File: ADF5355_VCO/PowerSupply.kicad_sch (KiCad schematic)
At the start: 15 parts, among them IC1 ADM7150ACPZ-3.3-R7, IC2 ADM7150ARDZ-5.0, U3 TPS7A0533PDBZ

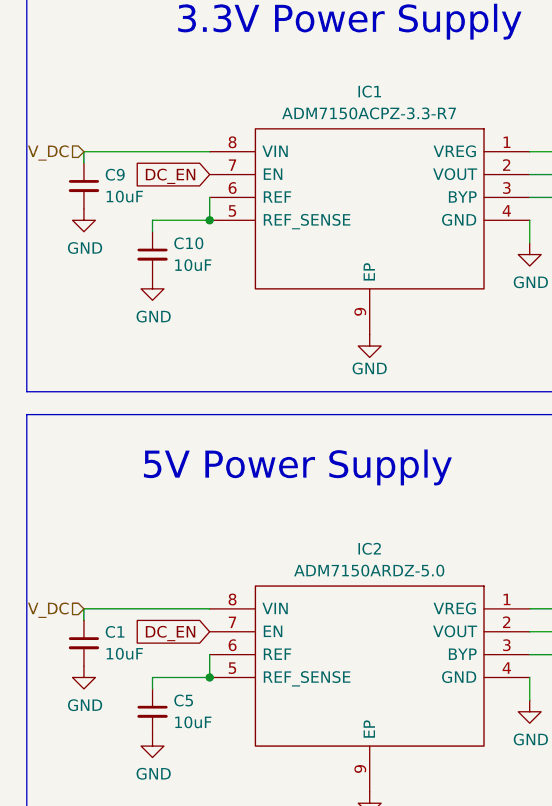
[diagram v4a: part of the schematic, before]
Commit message: Added additional footprints and BOM
Added a bill of materials with most of the components.
Added footprints for more components
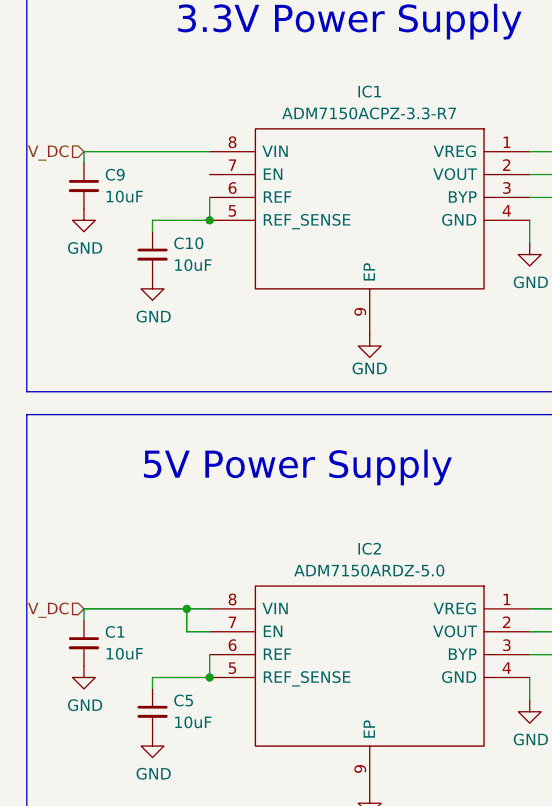
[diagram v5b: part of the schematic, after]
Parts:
- C1, C10, C11, C12, C2, C3, C4, C5, C6, C7, C8, C9: footprint (none) -> Capacitor_SMD:C_0603_1608Metric_Pad1.08x0.95mm_HandSolder
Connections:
- net V_DC: now also IC2.7 (EN)
- net DC_EN: no longer names the net of IC1.7 (EN)
- net DC_EN: no longer IC2.7 (EN)
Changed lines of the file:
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@@
   (junction (at 69.85 153.67) (diameter 0) (color 0 0 0 0)
   )
+  (junction (at 66.04 96.52) (diameter 0) (color 0 0 0 0)
+  )
   (wire (pts (xy 110.49 50.8) (xy 110.49 54.61))
     (stroke (width 0) (type default))
   )
+  (wire (pts (xy 66.04 96.52) (xy 54.61 96.52))
+    (stroke (width 0) (type default))
+  )
   (wire (pts (xy 69.85 161.29) (xy 69.85 165.1))
     (stroke (width 0) (type default))
@@
     (stroke (width 0) (type default))
   )
+  (wire (pts (xy 68.58 99.06) (xy 66.04 99.06))
+    (stroke (width 0) (type default))
+  )
   (wire (pts (xy 109.22 45.72) (xy 109.22 43.18))
     (stroke (width 0) (type default))
   )
-  (wire (pts (xy 68.58 96.52) (xy 54.61 96.52))
+  (wire (pts (xy 68.58 96.52) (xy 66.04 96.52))
     (stroke (width 0) (type default))
   )
@@
   )
   (wire (pts (xy 69.85 153.67) (xy 69.85 156.21))
+    (stroke (width 0) (type default))
+  )
+  (wire (pts (xy 66.04 99.06) (xy 66.04 96.52))
     (stroke (width 0) (type default))
   )
@@
     (effects (font (size 3 3)) (justify left bottom))
   )
-  (global_label "DC_EN" (shape input) (at 68.58 48.26 180) (fields_autoplaced)
-    (effects (font (size 1.27 1.27)) (justify right))
-    (property "Intersheetrefs" "${INTERSHEET_REFS}" (at 60.2619 48.26 0)
-      (effects (font (size 1.27 1.27)) (justify right) hide)
-    )
-  )
-  (global_label "DC_EN" (shape input) (at 68.58 99.06 180) (fields_autoplaced)
-    (effects (font (size 1.27 1.27)) (justify right))
-    (property "Intersheetrefs" "${INTERSHEET_REFS}" (at 60.2619 99.06 0)
-      (effects (font (size 1.27 1.27)) (justify right) hide)
-    )
-  )
   (hierarchical_label "VDDUSB" (shape input) (at 114.3 153.67 0) (fields_autoplaced)
     (effects (font (size 1.27 1.27)) (justify left))
@@
       (effects (font (size 1.27 1.27)) (justify left))
     )
-    (property "Footprint" "" (at 54.61 49.53 0)
+    (property "Footprint" "Capacitor_SMD:C_0603_1608Metric_Pad1.08x0.95mm_HandSolder" (at 54.61 49.53 0)
       (effects (font (size 1.27 1.27)) hide)
     )
@@
       (effects (font (size 1.27 1.27)) (justify left))
     )
-    (property "Footprint" "" (at 110.49 57.15 0)
+    (property "Footprint" "Capacitor_SMD:C_0603_1608Metric_Pad1.08x0.95mm_HandSolder" (at 110.49 57.15 0)
       (effects (font (size 1.27 1.27)) hide)
     )
@@
       (effects (font (size 1.27 1.27)) (justify left))
     )
-    (property "Footprint" "" (at 109.22 91.44 0)
+    (property "Footprint" "Capacitor_SMD:C_0603_1608Metric_Pad1.08x0.95mm_HandSolder" (at 109.22 91.44 0)
       (effects (font (size 1.27 1.27)) hide)
     )
@@
       (effects (font (size 1.27 1.27)) (justify left))
     )
-    (property "Footprint" "" (at 104.14 158.75 0)
+    (property "Footprint" "Capacitor_SMD:C_0603_1608Metric_Pad1.08x0.95mm_HandSolder" (at 104.14 158.75 0)
       (effects (font (size 1.27 1.27)) hide)
     )
@@
       (effects (font (size 1.27 1.27)) (justify left))
     )
-    (property "Footprint" "" (at 110.49 107.95 0)
+    (property "Footprint" "Capacitor_SMD:C_0603_1608Metric_Pad1.08x0.95mm_HandSolder" (at 110.49 107.95 0)
       (effects (font (size 1.27 1.27)) hide)
     )
@@
       (effects (font (size 1.27 1.27)) (justify left))
     )
-    (property "Footprint" "" (at 62.23 57.15 0)
+    (property "Footprint" "Capacitor_SMD:C_0603_1608Metric_Pad1.08x0.95mm_HandSolder" (at 62.23 57.15 0)
       (effects (font (size 1.27 1.27)) hide)
     )
@@
       (effects (font (size 1.27 1.27)) (justify left))
     )
-    (property "Footprint" "" (at 121.92 104.14 0)
+    (property "Footprint" "Capacitor_SMD:C_0603_1608Metric_Pad1.08x0.95mm_HandSolder" (at 121.92 104.14 0)
       (effects (font (size 1.27 1.27)) hide)
     )
@@
       (effects (font (size 1.27 1.27)) (justify left))
     )
-    (property "Footprint" "" (at 109.22 40.64 0)
+    (property "Footprint" "Capacitor_SMD:C_0603_1608Metric_Pad1.08x0.95mm_HandSolder" (at 109.22 40.64 0)
       (effects (font (size 1.27 1.27)) hide)
     )
@@
       (effects (font (size 1.27 1.27)) (justify left))
     )
-    (property "Footprint" "" (at 121.92 53.34 0)
+    (property "Footprint" "Capacitor_SMD:C_0603_1608Metric_Pad1.08x0.95mm_HandSolder" (at 121.92 53.34 0)
       (effects (font (size 1.27 1.27)) hide)
     )
@@
       (effects (font (size 1.27 1.27)) (justify left))
     )
-    (property "Footprint" "" (at 69.85 158.75 0)
+    (property "Footprint" "Capacitor_SMD:C_0603_1608Metric_Pad1.08x0.95mm_HandSolder" (at 69.85 158.75 0)
       (effects (font (size 1.27 1.27)) hide)
     )
@@
       (effects (font (size 1.27 1.27)) (justify left))
     )
-    (property "Footprint" "" (at 62.23 107.95 0)
+    (property "Footprint" "Capacitor_SMD:C_0603_1608Metric_Pad1.08x0.95mm_HandSolder" (at 62.23 107.95 0)
       (effects (font (size 1.27 1.27)) hide)
     )
@@
       (effects (font (size 1.27 1.27)) (justify left))
     )
-    (property "Footprint" "" (at 54.61 100.33 0)
-      (effects (font (size 1.27 1.27)) hide)
-    )
+    (property "Footprint" "Capacitor_SMD:C_0603_1608Metric_Pad1.08x0.95mm_HandSolder" (at 54.61 100.33 0)
+      (effects (font (size 1.27 1.27)) hide)
+    )

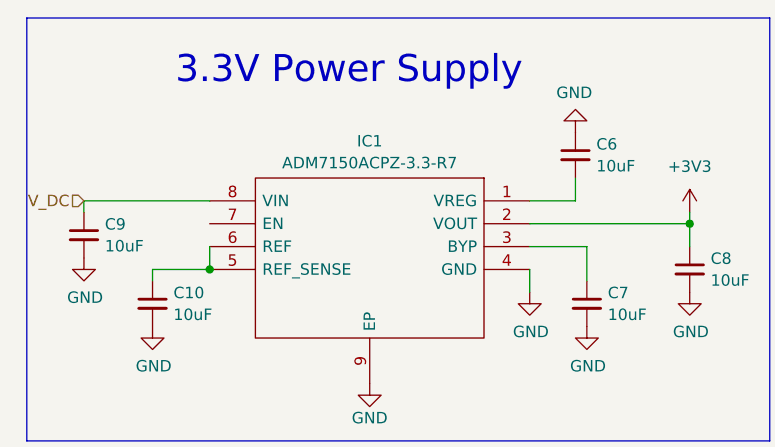
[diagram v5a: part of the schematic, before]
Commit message: Added TCXO and remaining footprints
Added remaining footprints
    NX3225GD
    710X toggle switch
    SMT button

Added ClearClock AX3 TCXO symbol and footprint

Added TCXO schematic with 3 options:
    LVPECL, LVDS and HCSL
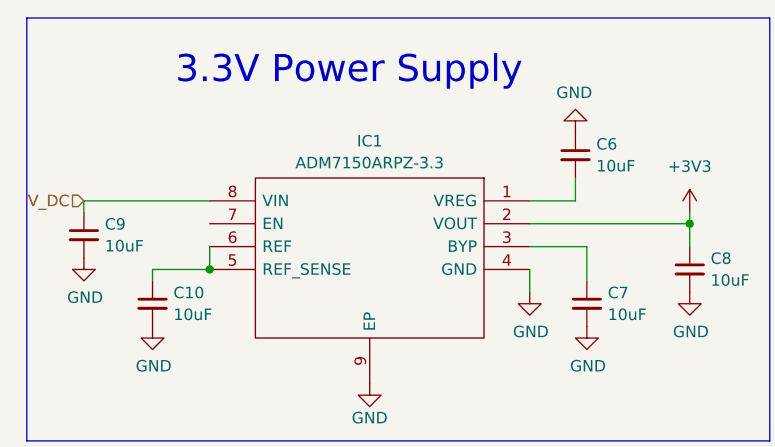
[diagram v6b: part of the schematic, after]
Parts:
- IC1: value ADM7150ACPZ-3.3-R7 -> ADM7150ARPZ-3.3; footprint SON50P300X300X85-9N-D -> Package_SO:SOIC-8-1EP_3.9x4.9mm_P1.27mm_EP2.41x3.3mm_ThermalVias
- IC2: footprint SOIC127P600X175-9N -> Package_SO:SOIC-8-1EP_3.9x4.9mm_P1.27mm_EP2.41x3.3mm_ThermalVias
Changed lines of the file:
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@@
       (effects (font (size 1.27 1.27)))
     )
-    (property "Footprint" "SOIC127P600X175-9N" (at 72.39 93.98 0)
+    (property "Footprint" "Package_SO:SOIC-8-1EP_3.9x4.9mm_P1.27mm_EP2.41x3.3mm_ThermalVias" (at 72.39 93.98 0)
       (effects (font (size 1.27 1.27)) (justify left) hide)
     )
@@
       (effects (font (size 1.27 1.27)))
     )
-    (property "Value" "ADM7150ACPZ-3.3-R7" (at 86.36 41.5107 0)
+    (property "Value" "ADM7150ARPZ-3.3" (at 86.36 41.5107 0)
       (effects (font (size 1.27 1.27)))
     )
-    (property "Footprint" "SON50P300X300X85-9N-D" (at 72.39 43.18 0)
+    (property "Footprint" "Package_SO:SOIC-8-1EP_3.9x4.9mm_P1.27mm_EP2.41x3.3mm_ThermalVias" (at 72.39 43.18 0)
       (effects (font (size 1.27 1.27)) (justify left) hide)
     )
